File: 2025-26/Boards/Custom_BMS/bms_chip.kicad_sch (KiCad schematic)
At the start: 51 parts, among them CN1 15246180, J7 Conn_01x06_Pin, Q1 BCX56-16,115, U1 BQ79616PAPRQ1

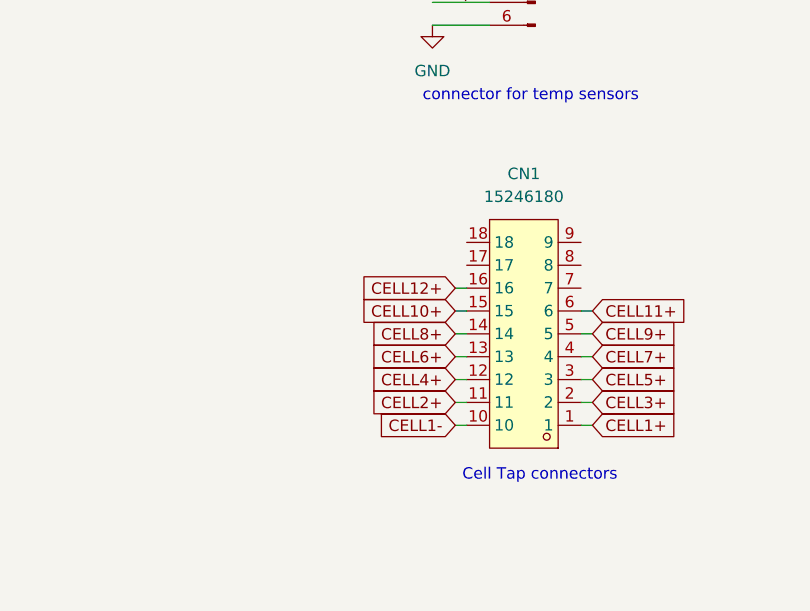
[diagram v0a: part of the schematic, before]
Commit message: layout fixes
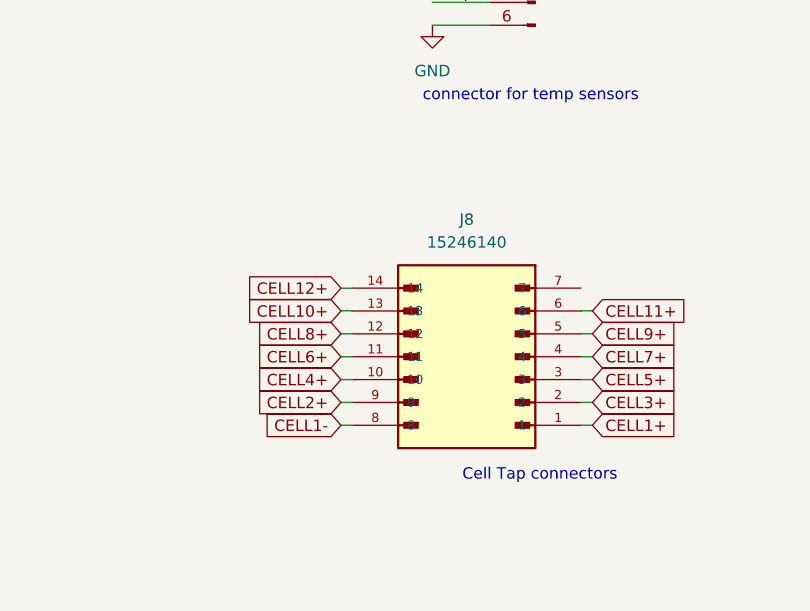
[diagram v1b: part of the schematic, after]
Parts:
- removed CN1: 15246180, easyeda2kicad:CONN-TH_15246180, symbol easyeda2kicad:15246180
- added J8: 15246140, easyeda2kicad:MOLEX_15246140, symbol 15246140:15246140
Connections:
- net CELL1+: now also J8.1
- net CELL1-: now also J8.8
- net CELL10+: now also J8.13
- net CELL11+: now also J8.6
- net CELL12+: now also J8.14
- net CELL2+: now also J8.9
- net CELL3+: now also J8.2
- net CELL4+: now also J8.10
- net CELL5+: now also J8.3
- net CELL6+: now also J8.11
- net CELL7+: now also J8.4
- net CELL8+: now also J8.12
- net CELL9+: now also J8.5
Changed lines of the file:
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@@
 	(wire
 		(pts
-			(xy 349.25 147.32) (xy 350.52 147.32)
+			(xy 336.55 147.32) (xy 337.82 147.32)
 		)
 		(stroke
@@
 	(wire
 		(pts
-			(xy 349.25 142.24) (xy 350.52 142.24)
+			(xy 336.55 142.24) (xy 337.82 142.24)
 		)
 		(stroke
@@
 	(wire
 		(pts
-			(xy 349.25 137.16) (xy 350.52 137.16)
+			(xy 336.55 137.16) (xy 337.82 137.16)
 		)
 		(stroke
@@
 	(wire
 		(pts
-			(xy 349.25 144.78) (xy 350.52 144.78)
+			(xy 336.55 144.78) (xy 337.82 144.78)
 		)
 		(stroke
@@
 	(wire
 		(pts
-			(xy 349.25 149.86) (xy 350.52 149.86)
+			(xy 336.55 149.86) (xy 337.82 149.86)
 		)
 		(stroke
@@
 	(wire
 		(pts
-			(xy 349.25 139.7) (xy 350.52 139.7)
+			(xy 336.55 139.7) (xy 337.82 139.7)
 		)
 		(stroke
@@
 	(wire
 		(pts
-			(xy 349.25 134.62) (xy 350.52 134.62)
+			(xy 336.55 134.62) (xy 337.82 134.62)
 		)
 		(stroke
@@
 	(global_label "CELL12+"
 		(shape input)
-		(at 349.25 134.62 180)
+		(at 336.55 134.62 180)
 		(fields_autoplaced yes)
 		(effects
@@
 		)
 		(property "Intersheetrefs" "${INTERSHEET_REFS}"
-			(at 337.7982 134.62 0)
+			(at 325.0982 134.62 0)
 			(effects
 				(font
@@
 	(global_label "CELL4+"
 		(shape input)
-		(at 349.25 144.78 180)
+		(at 336.55 144.78 180)
 		(fields_autoplaced yes)
 		(effects
@@
 		)
 		(property "Intersheetrefs" "${INTERSHEET_REFS}"
-			(at 339.0077 144.78 0)
+			(at 326.3077 144.78 0)
 			(effects
 				(font
@@
 	(global_label "CELL6+"
 		(shape input)
-		(at 349.25 142.24 180)
+		(at 336.55 142.24 180)
 		(fields_autoplaced yes)
 		(effects
@@
 		)
 		(property "Intersheetrefs" "${INTERSHEET_REFS}"
-			(at 339.0077 142.24 0)
+			(at 326.3077 142.24 0)
 			(effects
 				(font
@@
 	(global_label "CELL2+"
 		(shape input)
-		(at 349.25 147.32 180)
+		(at 336.55 147.32 180)
 		(fields_autoplaced yes)
 		(effects
@@
 		)
 		(property "Intersheetrefs" "${INTERSHEET_REFS}"
-			(at 339.0077 147.32 0)
+			(at 326.3077 147.32 0)
 			(effects
 				(font
@@
 	(global_label "CELL10+"
 		(shape input)
-		(at 349.25 137.16 180)
+		(at 336.55 137.16 180)
 		(fields_autoplaced yes)
 		(effects
@@
 		)
 		(property "Intersheetrefs" "${INTERSHEET_REFS}"
-			(at 337.7982 137.16 0)
+			(at 325.0982 137.16 0)
 			(effects
 				(font
@@
 	(global_label "CELL8+"
 		(shape input)
-		(at 349.25 139.7 180)
+		(at 336.55 139.7 180)
 		(fields_autoplaced yes)
 		(effects
@@
 		)
 		(property "Intersheetrefs" "${INTERSHEET_REFS}"
-			(at 339.0077 139.7 0)
+			(at 326.3077 139.7 0)
 			(effects
 				(font
@@
 	(global_label "CELL1-"
 		(shape input)
-		(at 349.25 149.86 180)
+		(at 336.55 149.86 180)
 		(fields_autoplaced yes)
 		(effects
@@
 		)
 		(property "Intersheetrefs" "${INTERSHEET_REFS}"
-			(at 339.0077 149.86 0)
+			(at 326.3077 149.86 0)
 			(effects
 				(font
@@
 	)
 	(symbol
-		(lib_id "easyeda2kicad:15246180")
-		(at 356.87 139.7 180)
-		(unit 1)
-		(exclude_from_sim no)
-		(in_bom yes)
-		(on_board yes)
-		(dnp no)
-		(property "Reference" "CN1"
-			(at 356.87 121.92 0)
-			(effects
-				(font
-					(size 1.27 1.27)
-				)
-			)
-		)
-		(property "Value" "15246180"
-			(at 356.87 124.46 0)
-			(effects
-				(font
-					(size 1.27 1.27)
-				)
-			)
-		)
-		(property "Footprint" "easyeda2kicad:CONN-TH_15246180"
-			(at 356.87 121.92 0)
-			(effects
-				(font
-					(size 1.27 1.27)
-				)
-				(hide yes)
-			)
-		)
-		(property "Datasheet" ""
-			(at 356.87 139.7 0)
-			(effects
-				(font
-					(size 1.27 1.27)
-				)
-				(hide yes)
-			)
-		)
-		(property "Description" ""
-			(at 356.87 139.7 0)
-			(effects
-				(font
-					(size 1.27 1.27)
-				)
-				(hide yes)
-			)
-		)
-		(property "LCSC Part" "C586535"
-			(at 356.87 119.38 0)
-			(effects
-				(font
-					(size 1.27 1.27)
-				)
-				(hide yes)
-			)
-		)
-		(pin "11"
-		)
-		(pin "2"
-		)
-		(pin "1"
-		)
-		(pin "3"
-		)
-		(pin "17"
-		)
-		(pin "14"
-		)
-		(pin "10"
-		)
-		(pin "13"
-		)
-		(pin "4"
-		)
-		(pin "18"
-		)
-		(pin "7"
-		)
-		(pin "9"
-		)
-		(pin "5"
-		)
-		(pin "15"
-		)
-		(pin "12"
-		)
-		(pin "6"
-		)
-		(pin "16"
-		)
-		(pin "8"
-		)
-		(instances
-			(project "Custom_BMS"
-				(path "/570d6d9c-ebf5-4f83-96f6-d3309a3e637d/730c9124-1e05-4e73-95cf-1be5bb1149a5"
-					(reference "CN1")
-					(unit 1)
-				)
-			)
-		)
-	)
-	(symbol
 		(lib_id "PCM_JLCPCB-Capacitors:0402,2.2uF")
 		(at 193.04 80.01 90)
@@
 					(unit 1)
 				)
+			)
+		)
+	)
+	(symbol
+		(lib_id "15246140:15246140")
+		(at 350.52 142.24 180)
+		(unit 1)
+		(exclude_from_sim no)
+		(in_bom yes)
+		(on_board yes)
+		(dnp no)
+		(fields_autoplaced yes)
+		(property "Reference" "J8"
+			(at 350.52 127 0)
+			(effects
+				(font
+					(size 1.27 1.27)
+				)
+			)
+		)
+		(property "Value" "15246140"
+			(at 350.52 129.54 0)
+			(effects
+				(font
+					(size 1.27 1.27)
+				)
+			)
+		)
+		(property "Footprint" "easyeda2kicad:MOLEX_15246140"
+			(at 350.52 142.24 0)
+			(effects
+				(font
+					(size 1.27 1.27)
+				)
+				(justify bottom)
+				(hide yes)
+			)
+		)
+		(property "Datasheet" ""
+			(at 350.52 142.24 0)
+			(effects
+				(font
+					(size 1.27 1.27)
+				)
+				(hide yes)
+			)
+		)
+		(property "Description" ""
+			(at 350.52 142.24 0)
+			(effects
+				(font
+					(size 1.27 1.27)
+				)
+				(hide yes)
+			)
+		)
+		(property "PARTREV" "T3"
+			(at 350.52 142.24 0)
+			(effects
+				(font
+					(size 1.27 1.27)
+				)
+				(justify bottom)
+				(hide yes)
+			)
+		)
+		(property "STANDARD" "Manufacturer Recommendations"
+			(at 350.52 142.24 0)
+			(effects
+				(font
+					(size 1.27 1.27)
+				)
+				(justify bottom)
+				(hide yes)
+			)
+		)
+		(property "MAXIMUM_PACKAGE_HEIGHT" "15mm"
+			(at 350.52 142.24 0)
+			(effects
+				(font
+					(size 1.27 1.27)
+				)
+				(justify bottom)
+				(hide yes)
+			)
+		)
+		(property "MANUFACTURER" "Molex"
+			(at 350.52 142.24 0)
+			(effects
+				(font
+					(size 1.27 1.27)
+				)
+				(justify bottom)
+				(hide yes)
+			)
+		)
+		(pin "7"
+		)
+		(pin "11"
+		)
+		(pin "4"
+		)
+		(pin "5"
+		)
+		(pin "12"
+		)
+		(pin "9"
+		)
+		(pin "6"
+		)
+		(pin "8"
+		)
+		(pin "10"
+		)
+		(pin "14"
+		)
+		(pin "13"
+		)
+		(pin "3"
+		)
+		(pin "2"
+		)
+		(pin "1"
+		)
+		(instances
+			(project ""
+				(path "/570d6d9c-ebf5-4f83-96f6-d3309a3e637d/730c9124-1e05-4e73-95cf-1be5bb1149a5"
+					(reference "J8")
+					(unit 1)
+				)

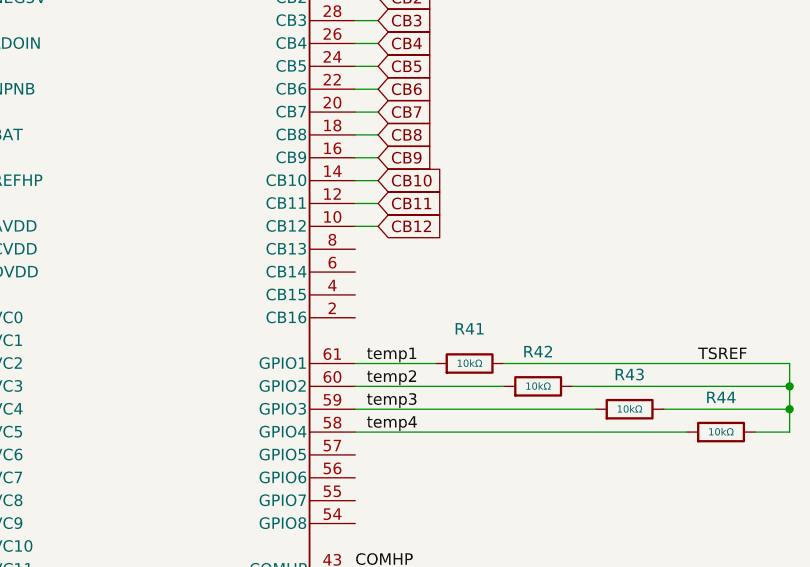
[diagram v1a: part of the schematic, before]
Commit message: fixed some layout and schematic issues
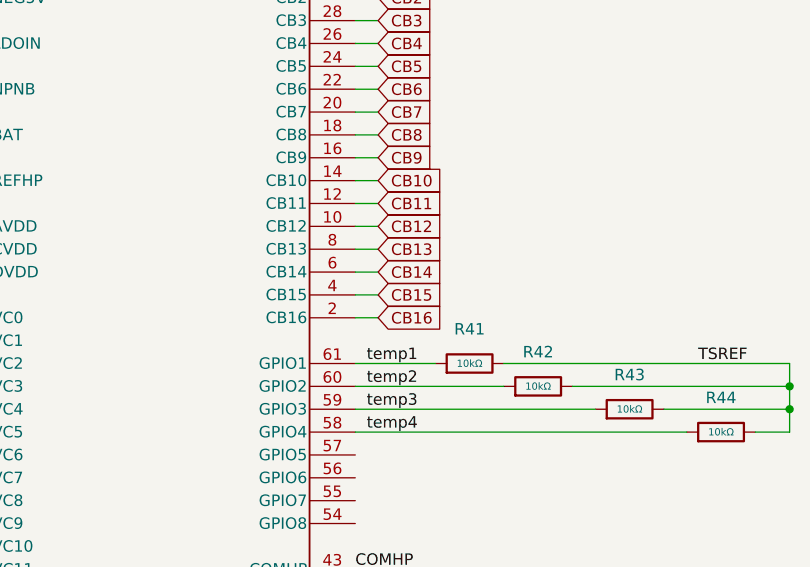
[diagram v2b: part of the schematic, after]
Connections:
- net CB16: now reaches U1.2 (CB16)
- net CB15: now reaches U1.4 (CB15)
- net CB14: now reaches U1.6 (CB14)
- net CB13: now reaches U1.8 (CB13)
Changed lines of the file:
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@@
 	(wire
 		(pts
+			(xy 267.97 80.01) (xy 265.43 80.01)
+		)
+		(stroke
+			(width 0)
+			(type default)
+		)
+	)
+	(wire
+		(pts
 			(xy 196.85 80.01) (xy 219.71 80.01)
 		)
@@
 	(wire
 		(pts
+			(xy 267.97 82.55) (xy 265.43 82.55)
+		)
+		(stroke
+			(width 0)
+			(type default)
+		)
+	)
+	(wire
+		(pts
 			(xy 217.17 87.63) (xy 219.71 87.63)
 		)
@@
 	(wire
 		(pts
+			(xy 267.97 85.09) (xy 265.43 85.09)
+		)
+		(stroke
+			(width 0)
+			(type default)
+		)
+	)
+	(wire
+		(pts
 			(xy 95.25 204.47) (xy 95.25 229.87)
 		)
@@
 	(wire
 		(pts
+			(xy 267.97 77.47) (xy 265.43 77.47)
+		)
+		(stroke
+			(width 0)
+			(type default)
+		)
+	)
+	(wire
+		(pts
 			(xy 217.17 90.17) (xy 219.71 90.17)
 		)
@@
 		)
 	)
+	(global_label "CB13"
+		(shape input)
+		(at 267.97 77.47 0)
+		(fields_autoplaced yes)
+		(effects
+			(font
+				(size 1.27 1.27)
+			)
+			(justify left)
+		)
+		(property "Intersheetrefs" "${INTERSHEET_REFS}"
+			(at 275.9142 77.47 0)
+			(effects
+				(font
+					(size 1.27 1.27)
+				)
+				(justify left)
+				(hide yes)
+			)
+		)
+	)
 	(global_label "CELL12+"
 		(shape input)
@@
 		)
 	)
+	(global_label "CB14"
+		(shape input)
+		(at 267.97 80.01 0)
+		(fields_autoplaced yes)
+		(effects
+			(font
+				(size 1.27 1.27)
+			)
+			(justify left)
+		)
+		(property "Intersheetrefs" "${INTERSHEET_REFS}"
+			(at 275.9142 80.01 0)
+			(effects
+				(font
+					(size 1.27 1.27)
+				)
+				(justify left)
+				(hide yes)
+			)
+		)
+	)
 	(global_label "CELL10+"
 		(shape input)
@@
 		)
 	)
+	(global_label "CB15"
+		(shape input)
+		(at 267.97 82.55 0)
+		(fields_autoplaced yes)
+		(effects
+			(font
+				(size 1.27 1.27)
+			)
+			(justify left)
+		)
+		(property "Intersheetrefs" "${INTERSHEET_REFS}"
+			(at 275.9142 82.55 0)
+			(effects
+				(font
+					(size 1.27 1.27)
+				)
+				(justify left)
+				(hide yes)
+			)
+		)
+	)
 	(global_label "CELL1-"
 		(shape input)
@@
 				(hide yes)
 			)
+		)
+	)
+	(global_label "CB16"
+		(shape input)
+		(at 267.97 85.09 0)
+		(fields_autoplaced yes)
+		(effects
+			(font
+				(size 1.27 1.27)
+			)
+			(justify left)
+		)
+		(property "Intersheetrefs" "${INTERSHEET_REFS}"
+			(at 275.9142 85.09 0)
+			(effects
+				(font
+					(size 1.27 1.27)
+				)
+				(justify left)
+				(hide yes)
+			)

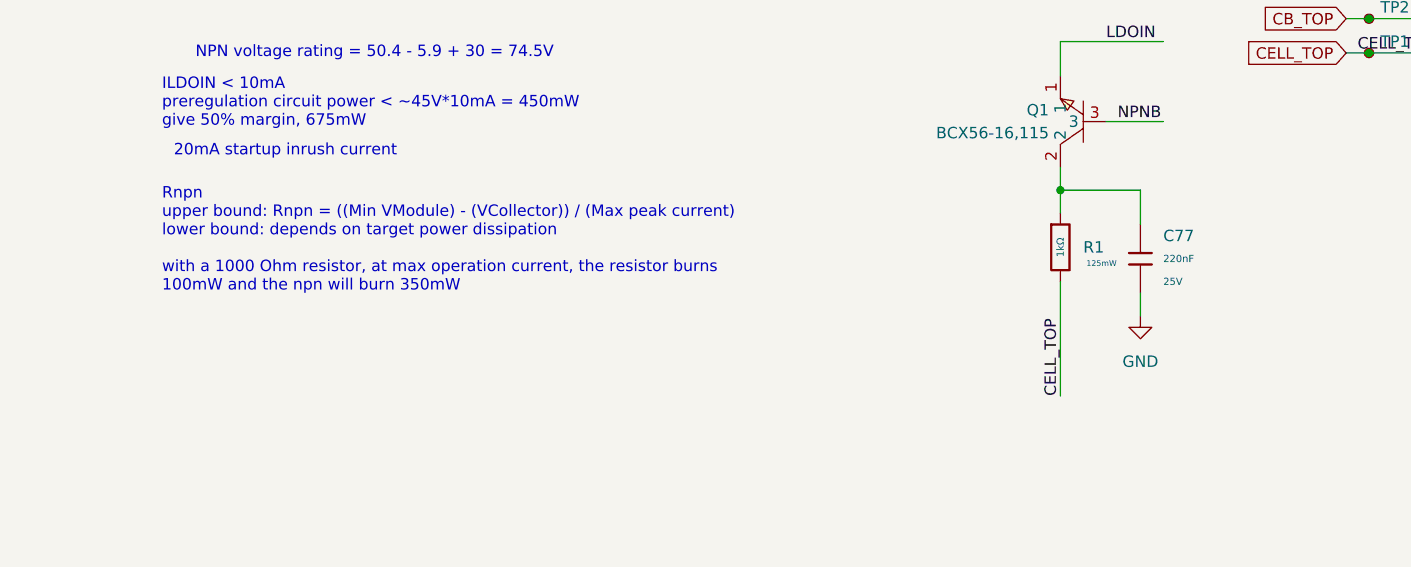
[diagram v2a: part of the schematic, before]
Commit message: started edits after PI suggestions
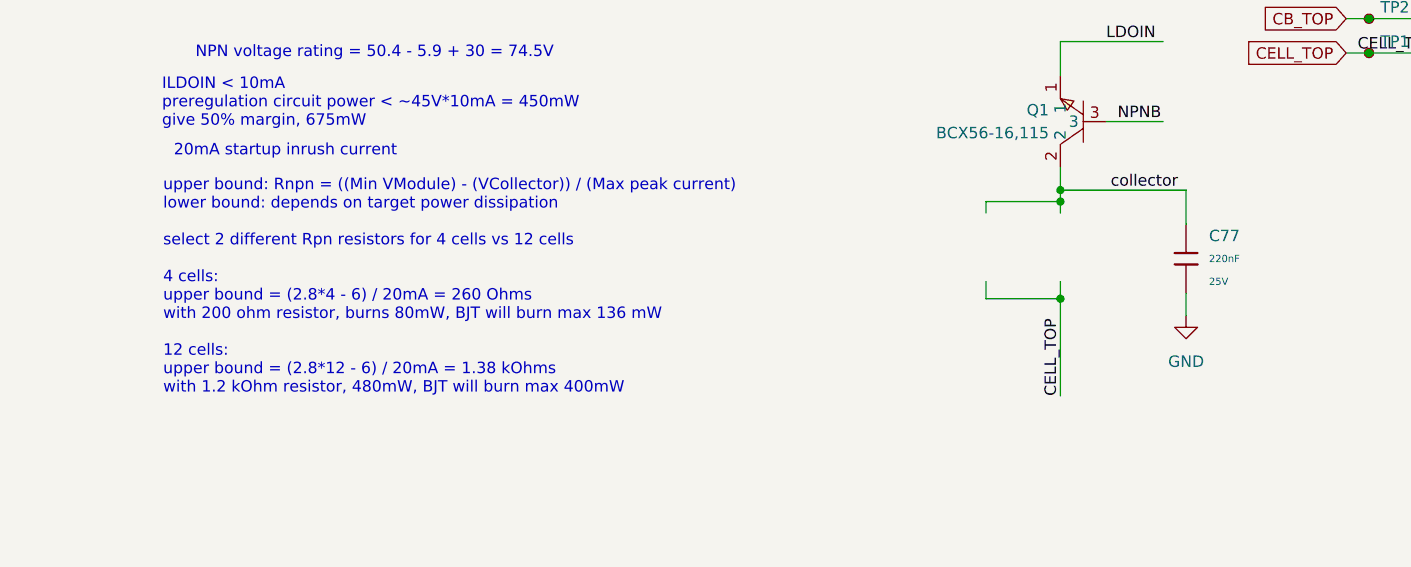
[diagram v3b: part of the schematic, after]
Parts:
- removed R1: 1kΩ, PCM_JLCPCB:R_0805, symbol PCM_JLCPCB-Resistors:0805,1kΩ
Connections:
- net collector: now reaches C77.1, Q1.2
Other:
- note added: "upper bound: Rnpn = ((Min VModule) - (VCollector)) / (Max peak current) lower bound: depends on target power dissipation select 2 different Rpn resistors for 4 cells vs 12 cells 4 cells: upper bound = (2.8*4 - 6) / 20mA = 260 Ohms with 200 ohm resistor, burns 80mW, BJT will burn max 136 mW 12 cells: upper bound = (2.8*12 - 6) / 20mA = 1.38 kOhms with 1.2 kOhm resistor, 480mW, BJT will burn max 40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"
- note removed: "Rnpn upper bound: Rnpn = ((Min VModule) - (VCollector)) / (Max peak current) lower bound: depends on target power dissipation with a 1000 Ohm resistor, at max operation current, the resistor burns 100mW and the npn will burn 350mW"
- moved on the sheet: C77

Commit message: fixed review items
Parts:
- removed Q1: BCX56-16,115, easyeda2kicad:SOT-89-3_L4.5-W2.5-P1.50-LS4.1-TL-CW, symbol easyeda2kicad:BCX56-16,115
- added JP3: SolderJumper_2_Bridged, Jumper:SolderJumper-2_P1.3mm_Open_Pad1.0x1.5mm, symbol Jumper:SolderJumper_2_Bridged
- added JP4: SolderJumper_2_Open, Jumper:SolderJumper-2_P1.3mm_Open_Pad1.0x1.5mm, symbol Jumper:SolderJumper_2_Open
- added Q1: ZXTN4004KTC, easyeda2kicad:TO-252-2_L6.6-W6.1-P4.58-LS9.9-TL, symbol easyeda2kicad:ZXTN4004KTC
- added R1, R77: 100Ω, PCM_JLCPCB:R_0805, symbol PCM_JLCPCB-Resistors:0805,100Ω
- added R78, R79: AC1210FR-07590RL, easyeda2kicad:R1210, symbol easyeda2kicad:AC1210FR-07590RL
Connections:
- net CELL_TOP: now also R77.2, R79.1
- net LDOIN: now also Q1.3 (E)
- net NPNB: now also Q1.1 (B)
- net collector: now also JP3.2 (B), JP4.2 (B), Q1.2 (C)
- new net: R1.2, R77.1
- new net: JP4.1 (A), R78.2
- new net: JP3.1 (A), R1.1
- new net: R78.1, R79.2
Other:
- note added: "12 cell option"
- note added: "4 cell option"
- note added: "BJT thermals- need enough copper area to be true"
- note added: "upper bound: Rnpn = ((Min VModule) - (VCollector)) / (Max peak current) lower bound: depends on target power dissipation select 2 different Rpn resistors for 4 cells vs 12 cells 4 cells: upper bound = (2.5*4 - 6) / 20mA = 200 Ohms with 200 ohm resistor, burns 80mW, BJT will burn max 136 mW 12 cells: upper bound = (2.5*12 - 6) / 20mA = 1.2 kOhms with 1.2 kOhm resistor, burns 480mW, BJT will burn m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"
- note removed: "upper bound: Rnpn = ((Min VModule) - (VCollector)) / (Max peak current) lower bound: depends on target power dissipation select 2 different Rpn resistors for 4 cells vs 12 cells 4 cells: upper bound = (2.8*4 - 6) / 20mA = 260 Ohms with 200 ohm resistor, burns 80mW, BJT will burn max 136 mW 12 cells: upper bound = (2.8*12 - 6) / 20mA = 1.38 kOhms with 1.2 kOhm resistor, 480mW, BJT will burn max 40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"
- moved on the sheet: C77
